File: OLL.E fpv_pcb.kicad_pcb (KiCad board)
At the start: 6 copper layers, 47.6 x 41.5 mm, 130 parts, among them J1 Micro_SD_Card, J10 Conn_01x05_Pin, J2 RC, J8 reciver, J9 TYPE-C-31-M-12, M1 M1 front left, M2 M2 front right, M3 M3 rear right, M4 m4 rear left, Q1 2N7002, SW1 SW_SPST, SW2 SW_SPST, U1 MP2315GJ, U10 AON7410, U11 UCC27511ADBV, U12 AON7410, U13 BMP280, U14 STM32H753VITx, U15 USBLC6-2SC6, U3 MP2315GJ, U4 ICM-42688-P, U5 UCC27511ADBV, U6 ul_AON7410, U7 UCC27511ADBV, U8 AON7410, U9 UCC27511ADBV, Y2 8HMz

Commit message: update
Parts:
- removed C15: 10uF, Capacitor_SMD:C_0603_1608Metric
- removed C22, C44: 10uF/25v, Capacitor_SMD:C_0603_1608Metric
- added C13: 100nF, Capacitor_SMD:C_0603_1608Metric, B.Cu at (138.4, 107.3)
- added D9: BZX84C10, Package_TO_SOT_SMD:SOT-23, B.Cu at (135.4, 107.0)
- added Q2: SUD45P03-09, Package_TO_SOT_SMD:TO-252-2, B.Cu at (177.4, 88.7)
- added R33: 100k, Resistor_SMD:R_0603_1608Metric, F.Cu at (153.2, 88.4)
- added R34: 33k, Resistor_SMD:R_0603_1608Metric, F.Cu at (150.9, 93.4)
- added R7: 0 ohm, Resistor_SMD:R_0603_1608Metric, B.Cu at (179.8, 80.5)
- C14: value 10uF -> 100nF
- C19: value 0.1µF -> 100nF
- C42, C43: value 12pF -> 15pF
- R1, R10: value 75k -> 100k
- REF**: value ESD-Logo_2.6mm_SilkScreen -> ESD-Logo_6.6x6mm_SilkScreen
- moved C14 10.5 mm to (153.4, 96.6), turned to 90 degrees
- moved U4 4.76 mm to (159.6, 100.9)
- moved REF** 3.96 mm to (156.9, 103.1)
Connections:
- BAT1 pad 1: +VBAT -> /VBAT_RAW
- C14 pad 1: +VBAT -> GND
- C14 pad 2: GND -> +VBAT
- R1 pad 1: Net-(R1-+) -> +VBAT
- R1 pad 2: GND -> Net-(R1--)
- R10 pad 1: Net-(R10-+) -> Net-(C13-+)
- U1 pad 1: Net-(R1-+) -> Net-(C8-+)
- U1 pad 6: +5V_FC -> Net-(R33-+)
- U14 pad 13: Net-(C43-+) -> Net-(R7--)
- U3 pad 1: Net-(R10-+) -> Net-(C19-+)
- U3 pad 6: +VBAT -> Net-(R1--)
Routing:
- net Net-(C13-+): track 0.00 -> 64.8 mm, vias 0 -> 4
- net GND: track 330.6 -> 393.9 mm, vias 33 -> 87
- net +VBAT: track 172.5 -> 110.9 mm, vias 9 -> 41
- net /VBAT_RAW: track 0.00 -> 56.2 mm, vias 0 -> 2
- net +3V3_FC: track 165.0 -> 201.6 mm, vias 14 -> 15
- net Net-(C43-+): track 12.8 -> 39.1 mm, vias 2 -> 3
- net Net-(R1--): track 0.00 -> 24.4 mm, vias 0 -> 3
- net Net-(R7--): track 0.00 -> 23.8 mm, vias 0 -> 2
- net C1_D0: track 66.3 -> 84.4 mm
- net Net-(R33-+): track 0.00 -> 8.58 mm, vias 0 -> 2
- net +5V_FC: track 180.4 -> 187.3 mm, vias 15 -> 16
- net SPI1_SDO: track 3.95 -> 10.7 mm
- net Net-(C8-+): track 13.7 -> 20.2 mm
- net SPI1_SDI: track 3.82 -> 10.3 mm
- net GYRO_CS: track 8.67 -> 14.8 mm
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- added copper zone on B.Cu, net +VBAT
- added copper zone on In2.Cu, net GND
- added copper zone on In3.Cu, net GND
- removed copper zone on F.Cu, net +3V3_FC

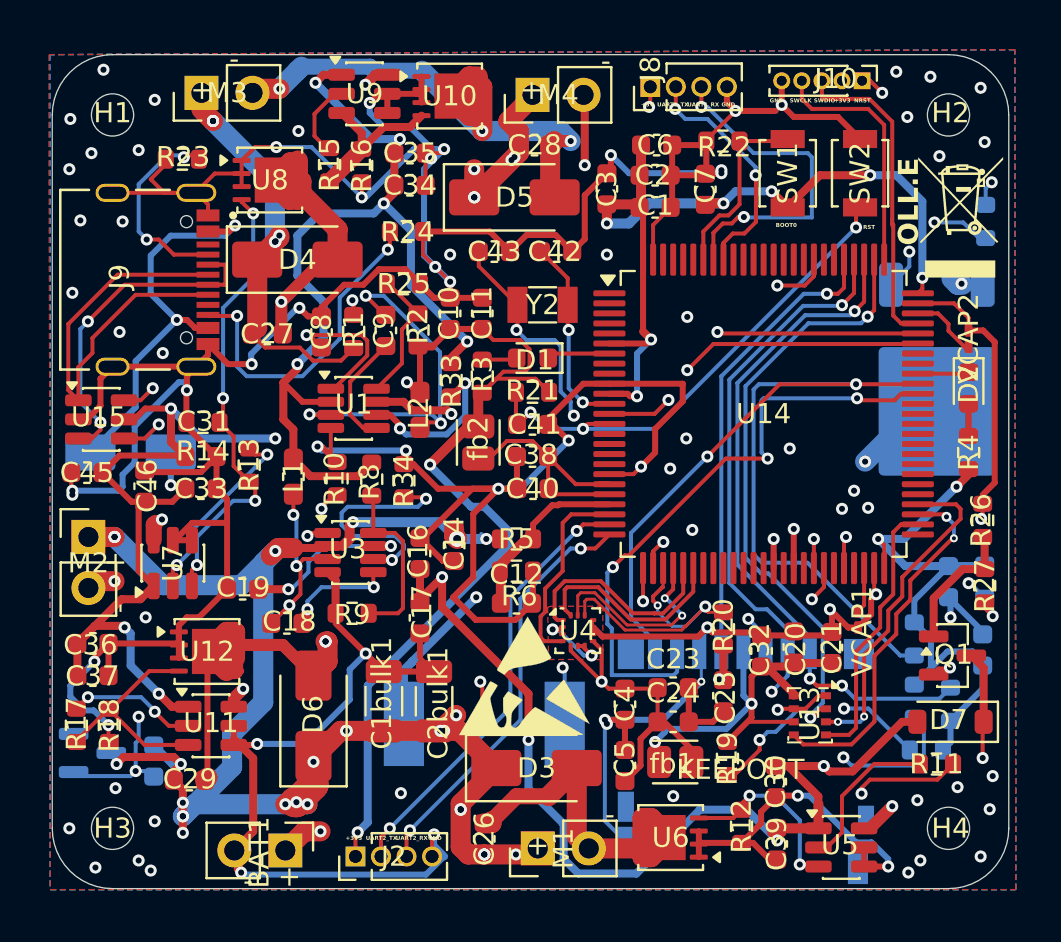
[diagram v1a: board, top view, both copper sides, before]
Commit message: update poller capictor 220uF/25
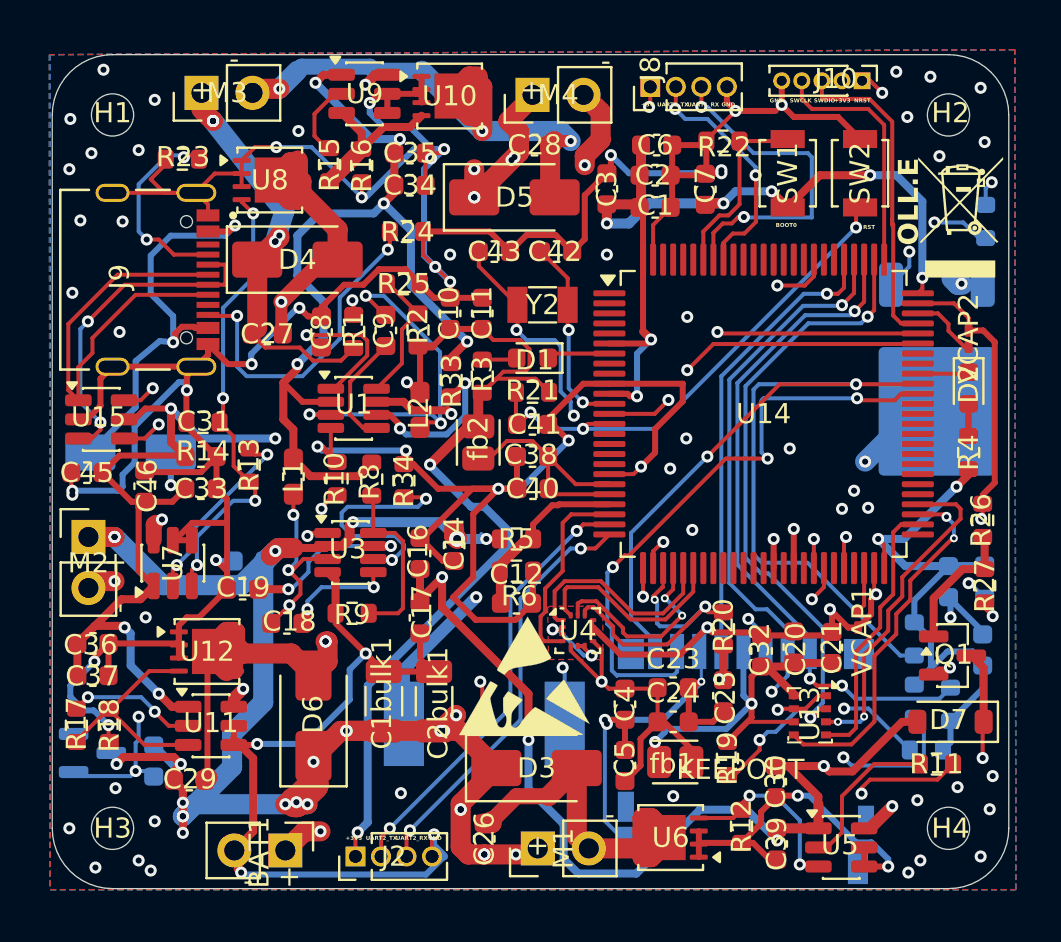
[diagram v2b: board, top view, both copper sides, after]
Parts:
- added C15: 10uF, Capacitor_SMD:C_0603_1608Metric, B.Cu at (143.2, 97.4)
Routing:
- net GND: track 393.9 -> 396.9 mm
- net +VBAT: track 110.9 -> 112.9 mm
- net Net-(C29--): track 56.1 -> 57.9 mm
- net VBUS: track 20.1 -> 21.1 mm
- net SPI1_SCK: track 10.1 -> 10.8 mm
- net Net-(C18--): track 9.08 -> 9.75 mm
- net +5V_FC: track 187.3 -> 186.7 mm

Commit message: latest scemetic
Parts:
- moved C15 0.35 mm to (142.9, 97.2)
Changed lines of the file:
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@@
 	(footprint "Capacitor_SMD:C_0603_1608Metric"
 		(layer "B.Cu")
-		(at 143.2 97.4 180)
+		(at 142.95 97.15 180)
 		(descr "Capacitor SMD 0603 (1608 Metric), square (rectangular) end terminal, IPC-7351 nominal, (Body size source: IPC-SM-782 page 76, https://www.pcb-3d.com/wordpress/wp-content/uploads/ipc-sm-782a_amendment_1_and_2.pdf), generated with kicad-footprint-generator")
 		(tags "capacitor")
@@
 		(start 151.85 81)
 		(end 151.85 82.15)
-		(width 0.2)
+		(width 0.4)
 		(layer "F.Cu")
 		(net 1)
@@
 		(start 141.15 79.655)
 		(end 140.57 79.075)
-		(width 0.2)
+		(width 0.3)
 		(layer "F.Cu")
 		(net 1)
@@
 		(start 142.825 77.465)
 		(end 143.49 76.8)
-		(width 0.2)
+		(width 0.3)
 		(layer "F.Cu")
 		(net 1)
@@
 		(start 151.85 82.15)
 		(end 153.2 83.5)
-		(width 0.2)
+		(width 0.4)
 		(layer "F.Cu")
 		(net 1)
@@
 		(start 143.49 76.8)
 		(end 144.55 76.8)
-		(width 0.2)
+		(width 0.3)
 		(layer "F.Cu")
 		(net 1)
@@
 		(start 141.15 80.2)
 		(end 141.15 79.655)
-		(width 0.2)
+		(width 0.3)
 		(layer "F.Cu")
 		(net 1)
@@
 		(start 140.57 79.03)
 		(end 141.485 78.115)
-		(width 0.2)
+		(width 0.3)
 		(layer "F.Cu")
 		(net 1)
@@
 	)
 	(segment
+		(start 173.8 112.6)
+		(end 175 112.6)
+		(width 0.3)
+		(layer "F.Cu")
+		(net 1)
+	)
+	(segment
 		(start 141.575 93.8)
 		(end 141.575 92.2)
@@
 		(start 142.825 77.465)
 		(end 142.825 78.765)
-		(width 0.2)
+		(width 0.3)
 		(layer "F.Cu")
 		(net 1)
@@
 		(start 151.975 77.1)
 		(end 152.7 77.1)
-		(width 0.2)
+		(width 0.4)
 		(layer "F.Cu")
 		(net 1)
@@
 	)
 	(segment
-		(start 173.8 112.6)
-		(end 175 112.6)
-		(width 0.3)
-		(layer "F.Cu")
-		(net 1)
-	)
-	(segment
 		(start 151.375 92.575)
 		(end 152.6 93.8)
@@
 		(start 164.175 79.8)
 		(end 163.3 80.675)
-		(width 0.2)
+		(width 0.3)
 		(layer "F.Cu")
 		(net 1)
@@
 	)
 	(segment
+		(start 163.3 82.4)
+		(end 163.3 80.675)
+		(width 0.3)
+		(layer "F.Cu")
+		(net 1)
+	)
+	(segment
 		(start 167.7 111.425)
 		(end 168.275 111.425)
@@
 	)
 	(segment
-		(start 163.3 80.675)
-		(end 163.3 82.4)
-		(width 0.2)
-		(layer "F.Cu")
-		(net 1)
-	)
-	(segment
 		(start 134.7 90.35)
 		(end 135.053052 90.35)
@@
 		(start 151.975 77.1)
 		(end 151.975 78.7)
-		(width 0.2)
+		(width 0.4)
 		(layer "F.Cu")
 		(net 1)
@@
 		(start 141.485 78.115)
 		(end 142.825 78.115)
-		(width 0.2)
+		(width 0.3)
 		(layer "F.Cu")
 		(net 1)
@@
 	)
 	(segment
-		(start 141.6 97.4)
-		(end 141.55 97.35)
-		(width 0.3)
-		(layer "B.Cu")
-		(net 1)
-	)
-	(segment
 		(start 136.9 93.1)
 		(end 136.9 93.7)
@@
 	)
 	(segment
+		(start 141.6 97.4)
+		(end 141.55 97.35)
+		(width 0.3)
+		(layer "B.Cu")
+		(net 1)
+	)
+	(segment
+		(start 142.175 97.15)
+		(end 141.925 97.4)
+		(width 0.3)
+		(layer "B.Cu")
+		(net 1)
+	)
+	(segment
 		(start 148.8 79.3)
 		(end 149 79.3)
@@
 	)
 	(segment
-		(start 142.425 97.4)
-		(end 141.6 97.4)
-		(width 0.3)
-		(layer "B.Cu")
-		(net 1)
-	)
-	(segment
 		(start 149.85 75.75)
 		(end 151.15 75.75)
@@
 	)
 	(segment
+		(start 141.925 97.4)
+		(end 141.6 97.4)
+		(width 0.3)
+		(layer "B.Cu")
+		(net 1)
+	)
+	(segment
 		(start 152.9 112.1)
 		(end 152 113)
@@
 	)
 	(segment
-		(start 142.8 98.6)
-		(end 144.5 96.9)
-		(width 1)
+		(start 139.9 109.425)
+		(end 139.9 110.1)
+		(width 0.4)
 		(layer "B.Cu")
 		(net 3)
 	)
 	(segment
-		(start 139.9 109.425)
-		(end 139.9 110.1)
-		(width 0.4)
+		(start 136.5 96.2)
+		(end 138.9 98.6)
+		(width 1)
 		(layer "B.Cu")
 		(net 3)
@@
 	)
 	(segment
-		(start 136.5 96.2)
-		(end 138.9 98.6)
-		(width 1)
-		(layer "B.Cu")
-		(net 3)
-	)
-	(segment
 		(start 139.8 107.5)
 		(end 139.375 107.5)
@@
 	)
 	(segment
-		(start 138.9 98.6)
-		(end 142.8 98.6)
-		(width 1)
-		(layer "B.Cu")
-		(net 3)
-	)
-	(segment
 		(start 178.15 83.35)
 		(end 178.45 83.65)
@@
 	)
 	(segment
+		(start 142.8 98.6)
+		(end 144.5 96.9)
+		(width 1)
+		(layer "B.Cu")
+		(net 3)
+	)
+	(segment
 		(start 144.95 80)
 		(end 144.48 81.52)
@@
 	)
 	(segment
+		(start 138.9 98.6)
+		(end 142.8 98.6)
+		(width 1)
+		(layer "B.Cu")
+		(net 3)
+	)
+	(segment
 		(start 136.6 107.2125)
 		(end 136.3375 106.95)
@@
 		(start 159.05 84.65)
 		(end 159.05 83.325)
-		(width 0.2)
+		(width 0.4)
 		(layer "F.Cu")
 		(net 19)
@@
 		(start 159.05 83.325)
 		(end 157.725 82)
-		(width 0.2)
+		(width 0.4)
 		(layer "F.Cu")
 		(net 19)
@@
 		(start 156.55 84.65)
 		(end 154.625 82.725)
-		(width 0.2)
+		(width 0.4)
 		(layer "F.Cu")
 		(net 20)
@@
 		(start 154.625 82.725)
 		(end 154.625 82)
-		(width 0.2)
+		(width 0.4)
 		(layer "F.Cu")
 		(net 20)
@@
 		(start 169.3 96.3)
 		(end 169.3 97.75)
-		(width 0.3)
+		(width 0.4)
 		(layer "F.Cu")
 		(net 62)
@@
 		(start 170.3 95.8)
 		(end 170.3 97.75)
-		(width 0.3)
+		(width 0.4)
 		(layer "F.Cu")
 		(net 63)
@@
 		(start 171.3 96.3)
 		(end 171.3 97.75)
-		(width 0.2)
+		(width 0.4)
 		(layer "F.Cu")
 		(net 64)
@@
 	)
 	(segment
-		(start 171.2 99.3)
-		(end 171.8 98.7)
-		(width 0.2)
+		(start 142.4375 104.22151)
+		(end 142.4375 104.65)
+		(width 0.6)
 		(layer "F.Cu")
 		(net 65)
 	)
 	(segment
-		(start 171.8 98.7)
-		(end 171.8 97.75)
-		(width 0.2)
+		(start 171.2 99.3)
+		(end 171.8 98.7)
+		(width 0.4)
 		(layer "F.Cu")
 		(net 65)
 	)
 	(segment
-		(start 142.4375 104.22151)
-		(end 142.4375 104.65)
+		(start 142.9 103.75901)
+		(end 142.4375 104.22151)
 		(width 0.6)
 		(layer "F.Cu")
@@
 	)
 	(segment
-		(start 142.9 103.75901)
-		(end 142.4375 104.22151)
-		(width 0.6)
+		(start 171.8 98.7)
+		(end 171.8 97.75)
+		(width 0.4)
 		(layer "F.Cu")
 		(net 65)

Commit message: update
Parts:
- removed C1bulk1, C2bulk1: 220uF/25v, Capacitor_SMD:C_1206_3216Metric
- added C22: 22uF, Capacitor_SMD:C_1210_3225Metric, B.Cu at (140.1, 111.3)
- added C44: 22uF, Capacitor_SMD:C_1210_3225Metric, B.Cu at (138.8, 100.0)
- added C49: 22uF, Capacitor_SMD:C_1210_3225Metric, B.Cu at (143.9, 76.6)
- added C50: 22uF, Capacitor_SMD:C_1210_3225Metric, B.Cu at (156.1, 78.4)
- added R35: 10k, Resistor_SMD:R_0603_1608Metric, B.Cu at (178.2, 80.5)
- added R36: 10k, Resistor_SMD:R_0603_1608Metric, B.Cu at (179.7, 95.4)
- added R37: 18 ohm, Resistor_SMD:R_0603_1608Metric, B.Cu at (154.7, 100.0)
- added R38: 20 ohm, Resistor_SMD:R_0603_1608Metric, B.Cu at (148.4, 86.0)
- added R39: 20 ohm, Resistor_SMD:R_0603_1608Metric, B.Cu at (149.0, 99.8)
- C18: moved to B.Cu
- moved C18 1.08 mm to (145.8, 99.8)
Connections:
- C9 pad 2: Net-(C9--) -> Net-(C9-+)
- D7 pad 2: +5V_FC -> Net-(D7-A)
- L1 pad 1: Net-(C18--) -> Net-(L1-+)
- L2 pad 1: Net-(C9--) -> Net-(L2-+)
- U1 pad 3: Net-(C9--) -> Net-(L2-+)
- U14 pad 47: unconnected-(U14-PB11-Pad47) -> Net-(R36-+)
- U14 pad 69: unconnected-(U14-PA10-Pad69) -> Net-(R35-+)
- U3 pad 3: Net-(C18--) -> Net-(L1-+)
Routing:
- net +VBAT: track 112.9 -> 142.4 mm
- net Net-(D7-A): track 0.00 -> 26.4 mm, vias 0 -> 2
- net Net-(C9--): track 18.8 -> 0.00 mm, vias 3 -> 0
- net GND: track 396.7 -> 411.7 mm, vias 87 -> 86
- net Net-(R36-+): track 0.00 -> 14.1 mm, vias 0 -> 2
- net Net-(L1-+): track 0.00 -> 12.8 mm, vias 0 -> 2
- net Net-(L2-+): track 0.00 -> 11.3 mm, vias 0 -> 1
- net Net-(R35-+): track 0.00 -> 8.84 mm, vias 0 -> 2
- net +5V_FC: track 186.7 -> 180.2 mm, vias 16 -> 15
- net Net-(C18--): track 9.75 -> 3.70 mm, vias 3 -> 0
- net Net-(C9-+): track 5.74 -> 10.4 mm, vias 0 -> 1
- net +3V3_FC: track 201.6 -> 204.9 mm
- net MOTOR3: track 40.6 -> 42.1 mm
- net Net-(C18-+): track 5.75 -> 4.45 mm, vias 2 -> 1
- net Net-(C19-+): track 12.8 -> 11.8 mm
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
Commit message: fixed all error
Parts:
- turned D7 to 0 degrees
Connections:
- C9 pad 2: Net-(C9-+) -> Net-(C9--)
- LS1 pad 1: Net-(D7-K) -> Net-(D7-A)
- LS1 pad 2: +5V_FC -> Net-(D7-K)
- Q1 pad 3: Net-(D7-K) -> Net-(D7-A)
- R37 pad 2: Net-(D7-A) -> Net-(D7-K)
- R38 pad 1: Net-(C9-+) -> Net-(C9--)
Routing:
- net +5V_FC: track 180.2 -> 172.4 mm
- net Net-(D7-A): track 26.4 -> 33.4 mm
- net Net-(C9-+): track 10.4 -> 5.74 mm, vias 1 -> 0
- net Net-(C9--): track 0.00 -> 2.13 mm, vias 0 -> 1
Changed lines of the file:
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@@
 	(net 15 "Net-(C29--)")
 	(net 16 "VDDA_FILT")
-	(net 17 "Net-(D7-K)")
+	(net 17 "Net-(D7-A)")
 	(net 18 "Net-(C42-+)")
 	(net 19 "Net-(C43-+)")
@@
 	(net 72 "unconnected-(U14-PE10-Pad40)")
 	(net 73 "unconnected-(U14-PD0-Pad81)")
-	(net 74 "Net-(D7-A)")
+	(net 74 "Net-(D7-K)")
 	(net 75 "unconnected-(U14-PC4-Pad32)")
 	(net 76 "unconnected-(U14-PC15-Pad9)")
@@
 	(net 130 "Net-(R35-+)")
 	(net 131 "Net-(R36-+)")
+	(net 132 "Net-(C9--)")
 	(footprint "Capacitor_SMD:C_0603_1608Metric"
 		(layer "F.Cu")
@@
 	(footprint "Diode_SMD:D_SOD-123"
 		(layer "F.Cu")
-		(at 178.1 105.4 180)
+		(at 178.1 105.4)
 		(descr "SOD-123")
 		(tags "SOD-123")
@@
 		)
 		(property "Datasheet" "https://www.vishay.com/docs/85748/1n4148w.pdf"
-			(at 0 0 180)
+			(at 0 0)
 			(unlocked yes)
 			(layer "F.Fab")
@@
 		)
 		(property "Description" "75V 0.15A Fast Switching Diode, SOD-123"
-			(at 0 0 180)
+			(at 0 0)
 			(unlocked yes)
 			(layer "F.Fab")
@@
 		)
 		(property "Sim.Device" "D"
-			(at 0 0 180)
+			(at 0 0)
 			(unlocked yes)
 			(layer "F.Fab")
@@
 		)
 		(property "Sim.Pins" "1=K 2=A"
-			(at 0 0 180)
+			(at 0 0)
 			(unlocked yes)
 			(layer "F.Fab")
@@
 		)
 		(pad "1" smd roundrect
-			(at -1.65 0 180)
+			(at -1.65 0)
 			(size 0.9 1.2)
 			(layers "F.Cu" "F.Mask" "F.Paste")
 			(roundrect_rratio 0.25)
-			(net 17 "Net-(D7-K)")
+			(net 74 "Net-(D7-K)")
 			(pinfunction "K")
 			(pintype "passive")
 		)
 		(pad "2" smd roundrect
-			(at 1.65 0 180)
+			(at 1.65 0)
 			(size 0.9 1.2)
 			(layers "F.Cu" "F.Mask" "F.Paste")
 			(roundrect_rratio 0.25)
-			(net 74 "Net-(D7-A)")
+			(net 17 "Net-(D7-A)")
 			(pinfunction "A")
 			(pintype "passive")
@@
 			(layers "F.Cu" "F.Mask" "F.Paste")
 			(roundrect_rratio 0.25)
-			(net 17 "Net-(D7-K)")
+			(net 17 "Net-(D7-A)")
 			(pinfunction "D")
 			(pintype "passive")
@@
 			(layers "F.Cu" "F.Mask" "F.Paste")
 			(roundrect_rratio 0.25)
-			(net 6 "Net-(C9-+)")
+			(net 132 "Net-(C9--)")
 			(pinfunction "-")
 			(pintype "passive")
@@
 			(layers "B.Cu" "B.Mask" "B.Paste")
 			(roundrect_rratio 0.25)
-			(net 74 "Net-(D7-A)")
+			(net 74 "Net-(D7-K)")
 			(pinfunction "-")
 			(pintype "passive")
@@
 			(size 2 4.2)
 			(layers "B.Cu" "B.Mask" "B.Paste")
-			(net 17 "Net-(D7-K)")
+			(net 17 "Net-(D7-A)")
 		)
 		(pad "2" smd rect
@@
 			(size 2 4.2)
 			(layers "B.Cu" "B.Mask" "B.Paste")
-			(net 8 "+5V_FC")
+			(net 74 "Net-(D7-K)")
 		)
 		(embedded_fonts no)
@@
 			(layers "B.Cu" "B.Mask" "B.Paste")
 			(roundrect_rratio 0.25)
-			(net 6 "Net-(C9-+)")
+			(net 132 "Net-(C9--)")
 			(pinfunction "+")
 			(pintype "passive")
@@
 	)
 	(segment
+		(start 150.9 102.925)
+		(end 152.825 101.0)
+		(width 0.4)
+		(layer "B.Cu")
+		(net 74)
+	)
+	(segment
+		(start 152.825 101.0)
+		(end 155.1 101.0)
+		(width 0.4)
+		(layer "B.Cu")
+		(net 74)
+	)
+	(segment
 		(start 180.3 86.5)
 		(end 180.3 93.5)
@@
 	)
 	(segment
-		(start 149.35 86.05)
-		(end 150 86.7)
-		(width 0.3)
-		(layer "F.Cu")
-		(net 6)
-	)
-	(segment
 		(start 148.875001 90.775)
 		(end 149.5375 90.775)
@@
 	)
 	(segment
-		(start 149.2 85.85)
-		(end 149.35 86)
-		(width 0.3)
-		(layer "F.Cu")
-		(net 6)
-	)
-	(segment
 		(start 148.225 88.475)
 		(end 148.225 90.124999)
@@
 		(width 0.2)
 		(layer "F.Cu")
-		(net 6)
+		(net 132)
 	)
 	(segment
@@
 		(width 0.2)
 		(layer "F.Cu")
-		(net 6)
-	)
-	(segment
-		(start 149.35 86)
-		(end 149.35 86.05)
-		(width 0.3)
-		(layer "F.Cu")
-		(net 6)
-	)
-	(segment
-		(start 149.093077 84.514281)
-		(end 149.2 84.621204)
-		(width 0.3)
-		(layer "F.Cu")
-		(net 6)
-	)
-	(segment
-		(start 149.2 84.621204)
-		(end 149.2 85.85)
-		(width 0.3)
-		(layer "F.Cu")
-		(net 6)
+		(net 132)
 	)
 	(segment
@@
 		(drill 0.3)
 		(layers "F.Cu" "B.Cu")
-		(net 6)
+		(net 132)
 	)
 	(segment
@@
 		(width 0.3)
 		(layer "B.Cu")
-		(net 6)
+		(net 132)
 	)
 	(segment
@@
 		(width 0.3)
 		(layer "B.Cu")
-		(net 6)
+		(net 132)
 	)
 	(segment
@@
 		(width 0.6)
 		(layer "B.Cu")
-		(net 8)
+		(net 74)
 	)
 	(segment
@@
 	)
 	(segment
-		(start 154.5 99.325)
-		(end 154.5 99.2)
-		(width 0.6)
-		(layer "B.Cu")
-		(net 8)
-	)
-	(segment
 		(start 139.3 92)
 		(end 139.3 93.525)
@@
 		(layer "B.Cu")
 		(net 8)
-	)
-	(segment
-		(start 150.9 102.925)
-		(end 154.5 99.325)
-		(width 0.6)
-		(layer "B.Cu")
-		(net 8)
